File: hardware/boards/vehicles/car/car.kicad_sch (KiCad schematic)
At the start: 22 parts, among them J1 Conn_01x04_Socket, J2 Conn_01x05_Socket, J3 Conn_01x05_Socket, J4 Conn_01x05_Socket, J5 Conn_01x02_Socket, SW1 SW_Push, U1 ATmega328P-A, Y1 8MHz

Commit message: REFACTO relinked every kicad projects
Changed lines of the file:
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@@
 	)
 	(junction
+		(at 95.25 120.65)
+		(diameter 0)
+		(color 0 0 0 0)
+	)
+	(junction
 		(at 218.44 36.83)
 		(diameter 0)
@@
 	(wire
 		(pts
-			(xy 208.28 39.37) (xy 218.44 39.37)
+			(xy 104.14 120.65) (xy 110.49 120.65)
 		)
 		(stroke
@@
 	(wire
 		(pts
-			(xy 105.41 120.65) (xy 110.49 120.65)
+			(xy 208.28 39.37) (xy 218.44 39.37)
 		)
 		(stroke
@@
 	(wire
 		(pts
+			(xy 104.14 102.87) (xy 95.25 102.87)
+		)
+		(stroke
+			(width 0)
+			(type default)
+		)
+	)
+	(wire
+		(pts
 			(xy 53.34 96.52) (xy 54.61 96.52)
 		)
@@
 	(wire
 		(pts
+			(xy 95.25 102.87) (xy 95.25 120.65)
+		)
+		(stroke
+			(width 0)
+			(type default)
+		)
+	)
+	(wire
+		(pts
 			(xy 100.33 127) (xy 100.33 125.73)
 		)
@@
 	(wire
 		(pts
+			(xy 104.14 120.65) (xy 104.14 102.87)
+		)
+		(stroke
+			(width 0)
+			(type default)
+		)
+	)
+	(wire
+		(pts
 			(xy 215.9 34.29) (xy 218.44 34.29)
 		)
@@
 			(at 38.1 29.21 0)
 			(effects
+				(font
+					(size 1.27 1.27)
+				)
+				(hide yes)
+			)
+		)
+		(property "Sim.Device" "V"
+			(at 38.1 29.21 0)
+			(effects
+				(font
+					(size 1.27 1.27)
+				)
+				(hide yes)
+			)
+		)
+		(property "Sim.Type" "DC"
+			(at 38.1 29.21 0)
+			(effects
+				(font
+					(size 1.27 1.27)
+				)
+				(hide yes)
+			)
+		)
+		(property "Sim.Pins" "1=+ 2=-"
+			(at 38.1 29.21 0)
+			(effects

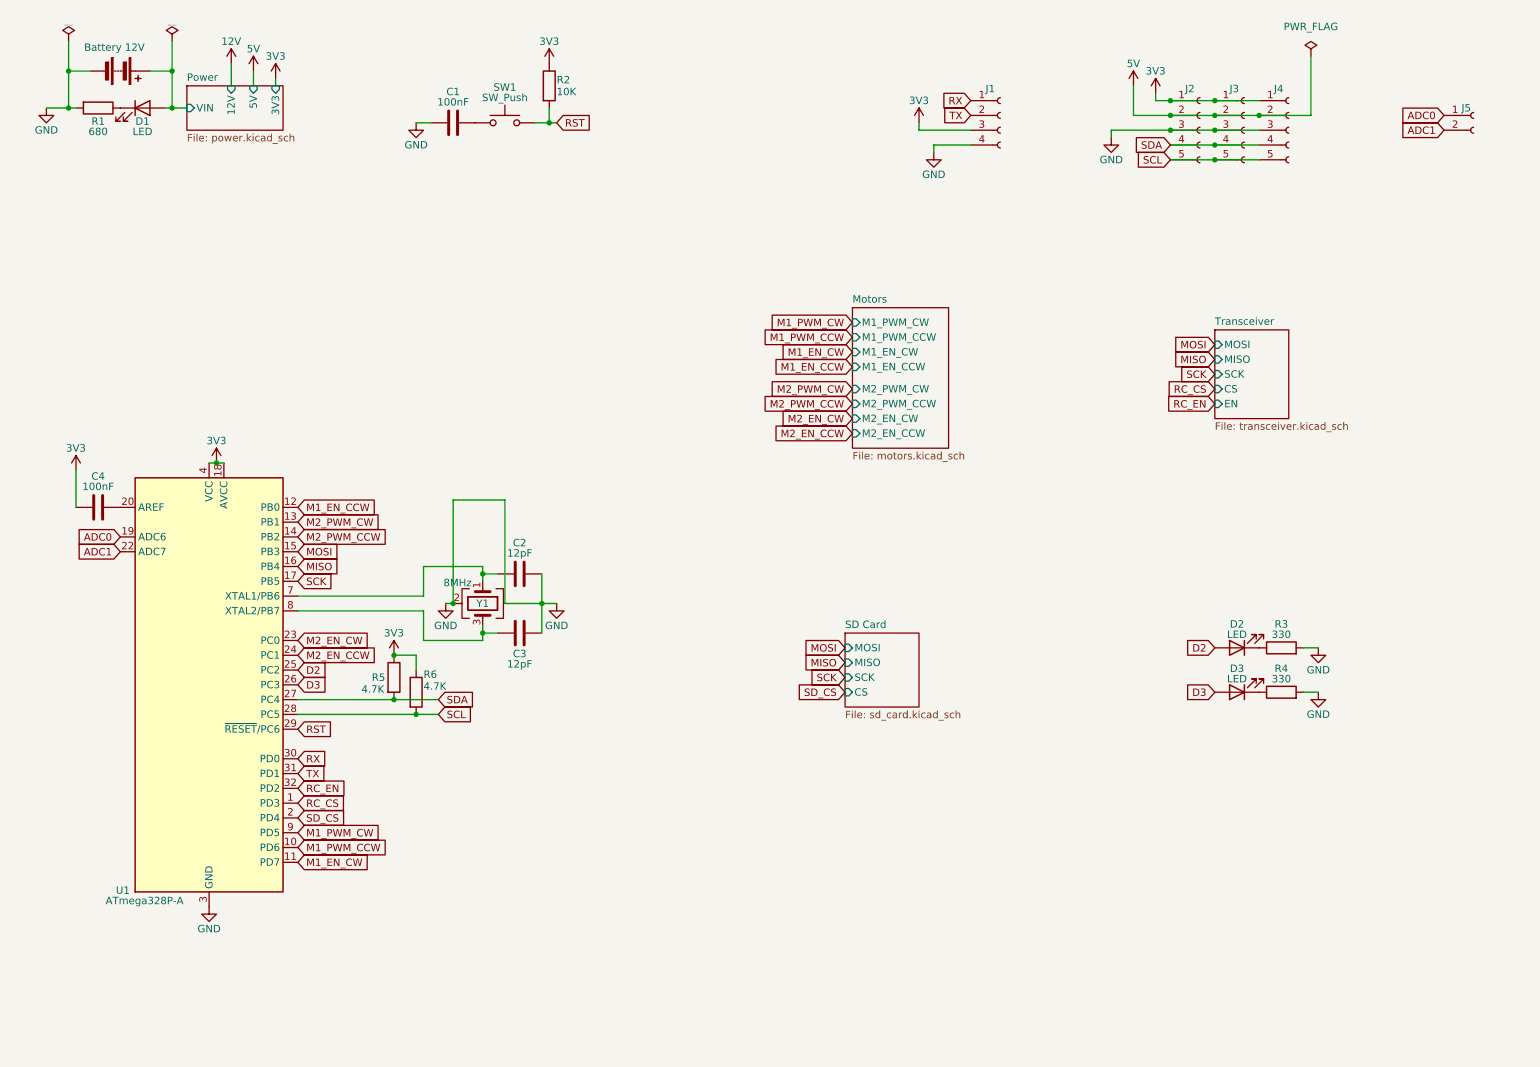
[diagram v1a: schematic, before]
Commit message: updated main points of the car schematic
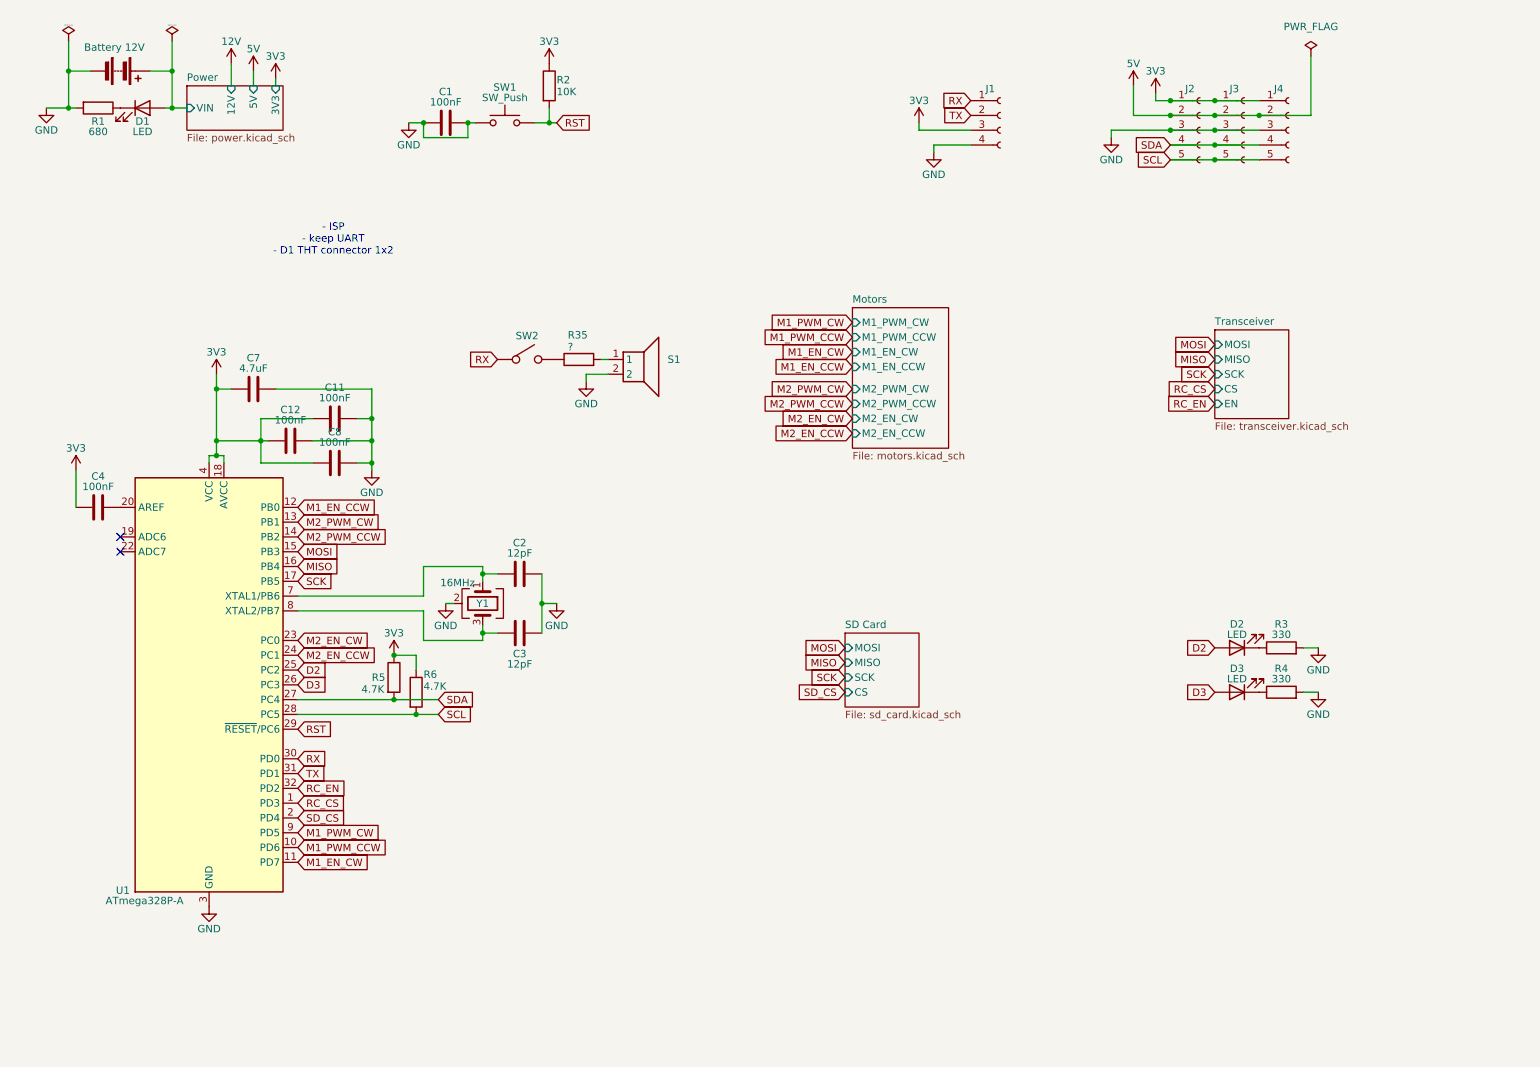
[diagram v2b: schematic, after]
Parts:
- removed J5: Conn_01x02_Socket, Connector_PinHeader_2.54mm:PinHeader_1x02_P2.54mm_Vertical, symbol Connector:Conn_01x02_Socket
- added C11, C12, C8: 100nF, Capacitor_SMD:C_0603_1608Metric_Pad1.08x0.95mm_HandSolder, symbol Device:C
- added C7: 4.7uF, Capacitor_SMD:C_0603_1608Metric_Pad1.08x0.95mm_HandSolder, symbol Device:C
- added R35: ?, Resistor_SMD:R_0603_1608Metric_Pad0.98x0.95mm_HandSolder, symbol Device:R
- added S1: ~, symbol common:SPEAKER
- added SW2: SW, switch:SW_Slide9.1x3.5, symbol common:Switch
- Y1: value 8MHz -> 16MHz
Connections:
- net 3V3: now also C11.1, C12.1, C7.1, C8.1
- net GND: now also C1.2, SW1.1, C11.2, C12.2, C7.2, C8.2, S1.2
- net RX: now also SW2.1
- net ADC0: no longer names the net of U1.19 (ADC6)
- net ADC1: no longer names the net of U1.22 (ADC7)
- new net: R35.1, SW2.2
- new net: R35.2, S1.1
- no-connect marks 0 -> 2
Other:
- note added: "- ISP - keep UART - D1 THT connector 1x2"
- moved on the sheet: C1

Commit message: car PCB
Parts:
- removed SW2: SW, switch:SW_Slide9.1x3.5, symbol common:Switch
- added J1: Dupont, Connector_PinHeader_2.54mm:PinHeader_1x06_P2.54mm_Vertical, symbol Connector:Conn_01x06_Socket
- added J3: Dupont, connector:Pin_02x04, symbol connector:Pin_02x04
- BT1: value Battery 12V -> JST; footprint Connector_PinHeader_2.54mm:PinHeader_1x02_P2.54mm_Vertical -> Connector_JST:JST_XH_B2B-XH-A_1x02_P2.50mm_Vertical
- BZ1: renamed from S1; value ~ -> Buzzer; footprint (none) -> common:buzzer_8.5x8.5
- D1, D3: value LED -> RED
- D2: value LED -> GREEN
- J2: renamed from J1; value Conn_01x04_Socket -> Dupont
- J4: renamed from J2; value Conn_01x05_Socket -> JST; footprint Connector_PinHeader_2.54mm:PinHeader_1x05_P2.54mm_Vertical -> Connector_JST:JST_XH_B5B-XH-A_1x05_P2.50mm_Vertical
- J5: renamed from J3; value Conn_01x05_Socket -> JST; footprint Connector_PinHeader_2.54mm:PinHeader_1x05_P2.54mm_Vertical -> Connector_JST:JST_XH_B5B-XH-A_1x05_P2.50mm_Vertical
- J6: renamed from J4; value Conn_01x05_Socket -> JST; footprint Connector_PinHeader_2.54mm:PinHeader_1x05_P2.54mm_Vertical -> Connector_JST:JST_XH_B5B-XH-A_1x05_P2.50mm_Vertical
- renumbered C7 to C4, C12 to C5, C11 to C6, C8 to C7, C4 to C8, R35 to R5, R5 to R6, R6 to R7
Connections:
- net Power/VIN is gone; now on net 12V: BT1.1 (+), D1.2 (A)
- net 3V3: now also J1.5 (Pin_5), J3.8
- net GND: now also J1.6 (Pin_6), J3.1
- net MISO: now also J1.2 (Pin_2), J3.4
- net MOSI: now also J1.3 (Pin_3), J3.6
- net RC_CS: now also J3.7
- net RC_EN: now also J3.2
- net RST: now also J1.4 (Pin_4)
- net RX: now also J2.2 (Pin_2), R5.1; no longer J2.1 (Pin_1)
- net SCK: now also J1.1 (Pin_1), J3.3
- net TX: now also J2.1 (Pin_1); no longer J2.2 (Pin_2)
- no-connect marks 2 -> 3
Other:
- removed sheet Transceiver
- sheet Power ports: added none; removed 12V
- note removed: "- ISP - keep UART - D1 THT connector 1x2"
- moved on the sheet: J2

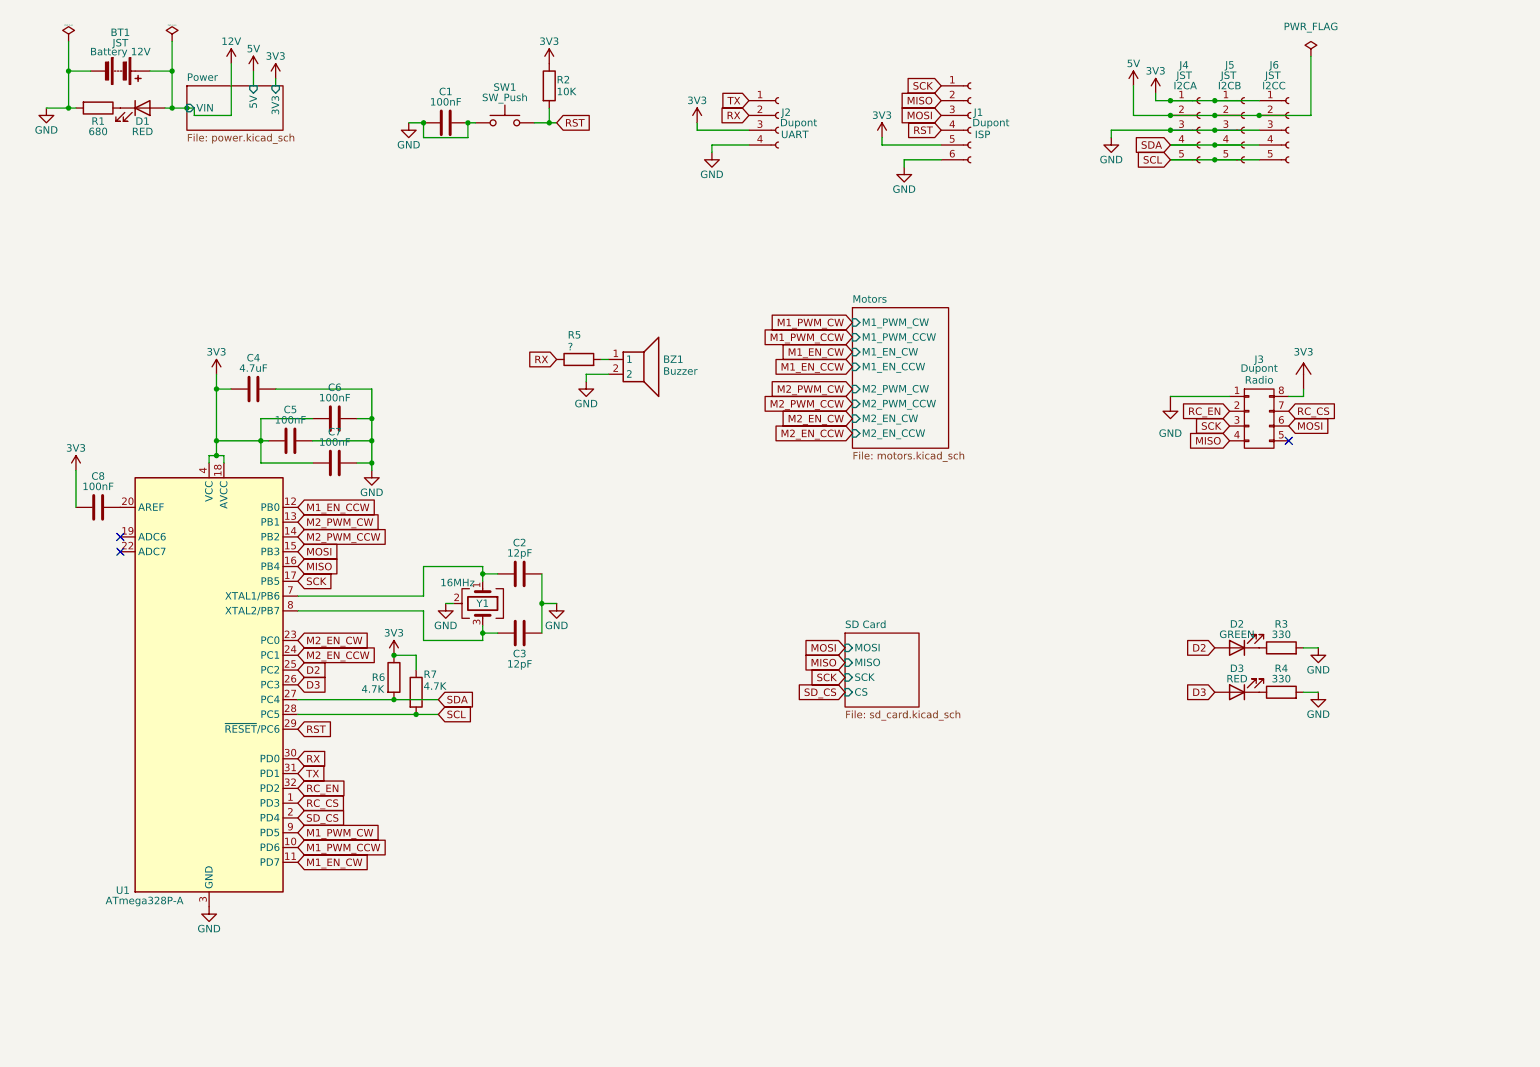
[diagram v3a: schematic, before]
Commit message: change kicad default to custom
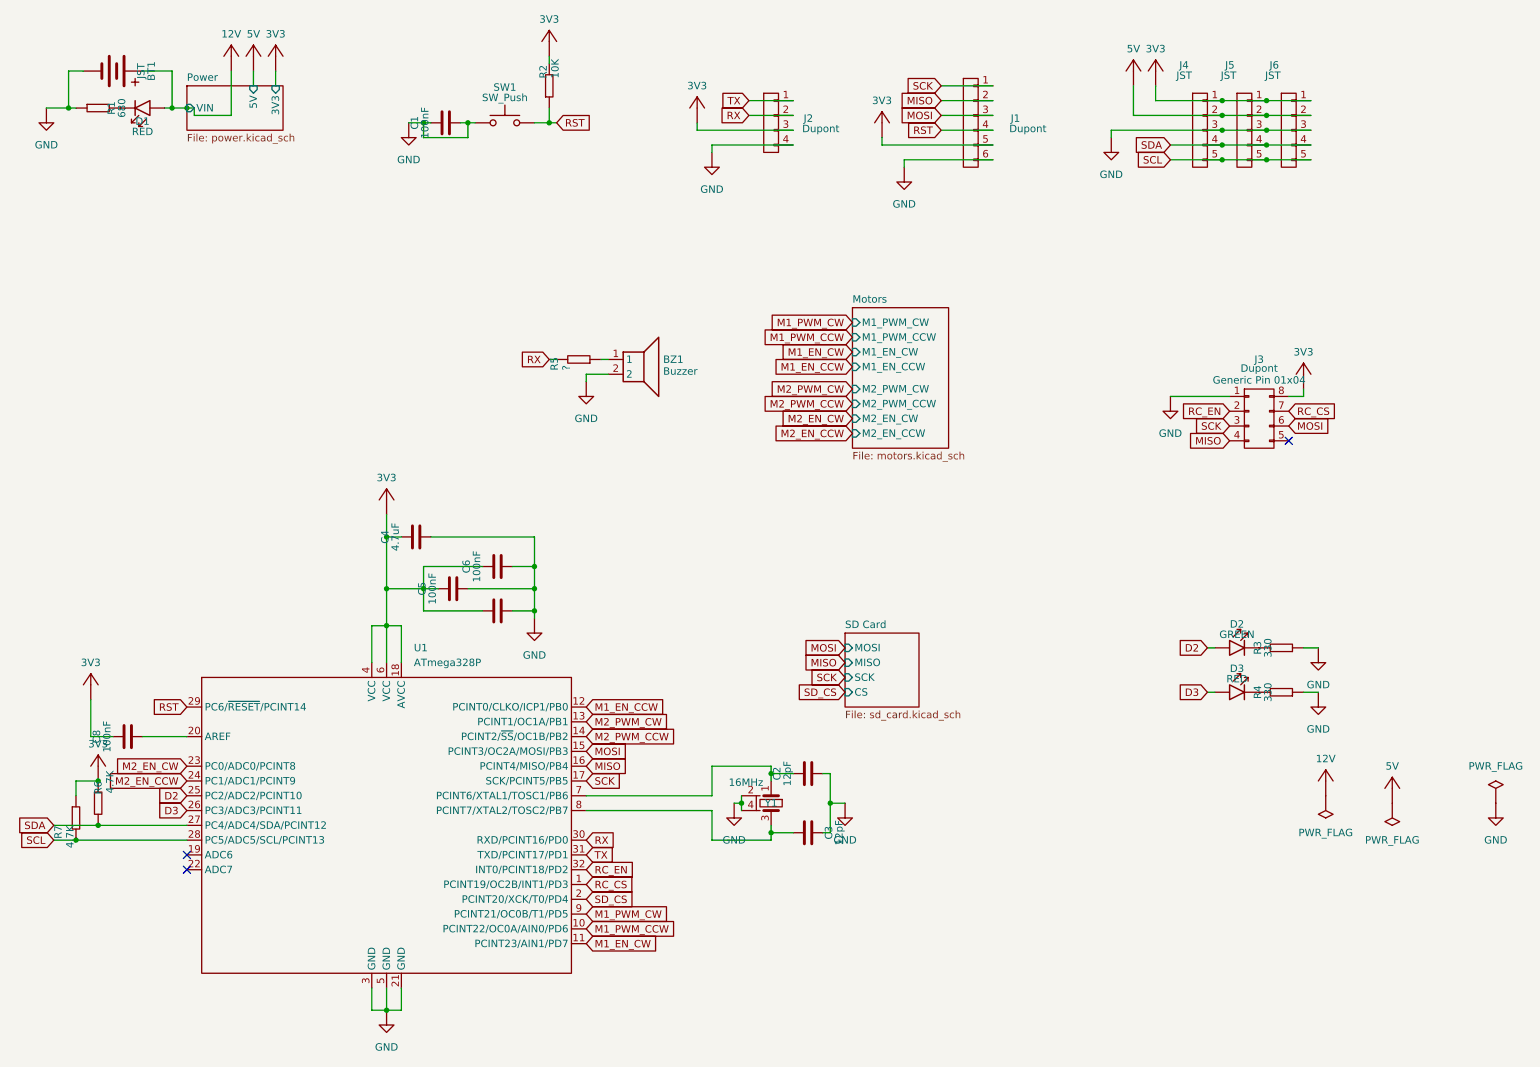
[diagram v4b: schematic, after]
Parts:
- removed U1: ATmega328P-A, Package_QFP:TQFP-32_7x7mm_P0.8mm, symbol MCU_Microchip_ATmega:ATmega328P-A
- added U1: ATmega328P, microchip:ATmega328p_TQFP, symbol microchip:ATmega328P
- BT1: footprint Connector_JST:JST_XH_B2B-XH-A_1x02_P2.50mm_Vertical -> connector:JST_1x2; symbol Device:Battery -> common:Battery
- C1, C2, C3, C4, C5, C6, C7, C8: footprint Capacitor_SMD:C_0603_1608Metric_Pad1.08x0.95mm_HandSolder -> common:C_0603; symbol Device:C -> common:Capacitor
- D1, D2, D3: footprint LED_SMD:LED_0603_1608Metric_Pad1.05x0.95mm_HandSolder -> common:LED_0603; symbol Device:LED -> common:LED
- J1: footprint Connector_PinHeader_2.54mm:PinHeader_1x06_P2.54mm_Vertical -> connector:Pin_01x06; symbol Connector:Conn_01x06_Socket -> connector:Pin_01x06
- J2: footprint Connector_PinHeader_2.54mm:PinHeader_1x04_P2.54mm_Vertical -> connector:Pin_01x04; symbol Connector:Conn_01x04_Socket -> connector:Pin_01x04
- J4, J5, J6: footprint Connector_JST:JST_XH_B5B-XH-A_1x05_P2.50mm_Vertical -> connector:JST_1x5; symbol Connector:Conn_01x05_Socket -> connector:Pin_01x05
- R1, R2, R3, R4, R5, R6, R7: footprint Resistor_SMD:R_0603_1608Metric_Pad0.98x0.95mm_HandSolder -> common:R_0603; symbol Device:R -> common:Resistor
- Y1: symbol Device:Crystal_GND24 -> common:Crystal_4Pins
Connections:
- net 3V3: now also C4.2, C5.2, C6.2, C7.2, C8.2, R2.2, U1.18 (AVCC), U1.4 (VCC), U1.6 (VCC); no longer C4.1, C5.1, C6.1, C7.1, C8.1, R2.1
- net D2: now also U1.25 (PC2/ADC2/PCINT10)
- net D3: now also U1.26 (PC3/ADC3/PCINT11)
- net GND: now also C2.1, C3.1, C4.1, C5.1, C6.1, C7.1, R1.1, R3.1, R4.1, U1.21 (GND), U1.3 (GND), U1.5 (GND); no longer C2.2, C3.2, C4.2, C5.2, C6.2, C7.2, R1.2, R3.2, R4.2
- net M1_EN_CCW: now also U1.12 (PCINT0/CLKO/ICP1/PB0)
- net M1_EN_CW: now also U1.11 (PCINT23/AIN1/PD7)
- net M1_PWM_CCW: now also U1.10 (PCINT22/OC0A/AIN0/PD6)
- net M1_PWM_CW: now also U1.9 (PCINT21/OC0B/T1/PD5)
- net M2_EN_CCW: now also U1.24 (PC1/ADC1/PCINT9)
- net M2_EN_CW: now also U1.23 (PC0/ADC0/PCINT8)
- net M2_PWM_CCW: now also U1.14 (PCINT2/~{SS}/OC1B/PB2)
- net M2_PWM_CW: now also U1.13 (PCINT1/OC1A/PB1)
- net MISO: now also U1.16 (PCINT4/MISO/PB4)
- net MOSI: now also U1.15 (PCINT3/OC2A/MOSI/PB3)
- net RC_CS: now also U1.1 (PCINT19/OC2B/INT1/PD3)
- net RC_EN: now also U1.32 (INT0/PCINT18/PD2)
- net RST: now also R2.1, U1.29 (PC6/~{RESET}/PCINT14); no longer R2.2
- net RX: now also R5.2, U1.30 (RXD/PCINT16/PD0); no longer R5.1
- net SCK: now also U1.17 (SCK/PCINT5/PB5)
- net SCL: now also U1.28 (PC5/ADC5/SCL/PCINT13)
- net SDA: now also U1.27 (PC4/ADC4/SDA/PCINT12)
- net SD_CS: now also U1.2 (PCINT20/XCK/T0/PD4)
- net TX: now also U1.31 (TXD/PCINT17/PD1)
- net at D2.1 (K): now also R3.2; no longer R3.1
- net at BZ1.1: now also R5.1; no longer R5.2
- net at D1.1 (K): now also R1.2; no longer R1.1
- net at Y1.3: now also C3.2, U1.8 (PCINT7/XTAL2/TOSC2/PB7); no longer C3.1
- net at Y1.1: now also C2.2, U1.7 (PCINT6/XTAL1/TOSC1/PB6); no longer C2.1
- net at D3.1 (K): now also R4.2; no longer R4.1
- new net: C8.1, U1.20 (AREF)
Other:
- moved on the sheet: C1, C2, C3, C4, C5, C6, C8, R1, R2, R3, R4, R5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
